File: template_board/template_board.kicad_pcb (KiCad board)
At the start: 4 copper layers, 100 x 60 mm, 150 parts, among them IC1 TJA1044GTK_3Z, IC2 TJA1044GTK_3Z, IC3 LMR16030SDDAR, J1 SWD, J2 Conn_01x02, J4 USB_C_Receptacle_USB2.0, J6 Conn_01x02, J7 RJ45_LED_Shielded, J8 RJ45_LED_Shielded, Q1 S9013, SW2 NRST, SW5 SW_DIP_x02, U1 CH334R, U2 FM24CL16B, U3 STM32F103CB, U4 AZ1117-3.3, U6 IP4220CZ6, U8 TS3USB30EDGSR, U9 STM32F446RETx, Y1 8MHz, Y2 8MHz, Y3 32.768kHz, Y4 12Mhz

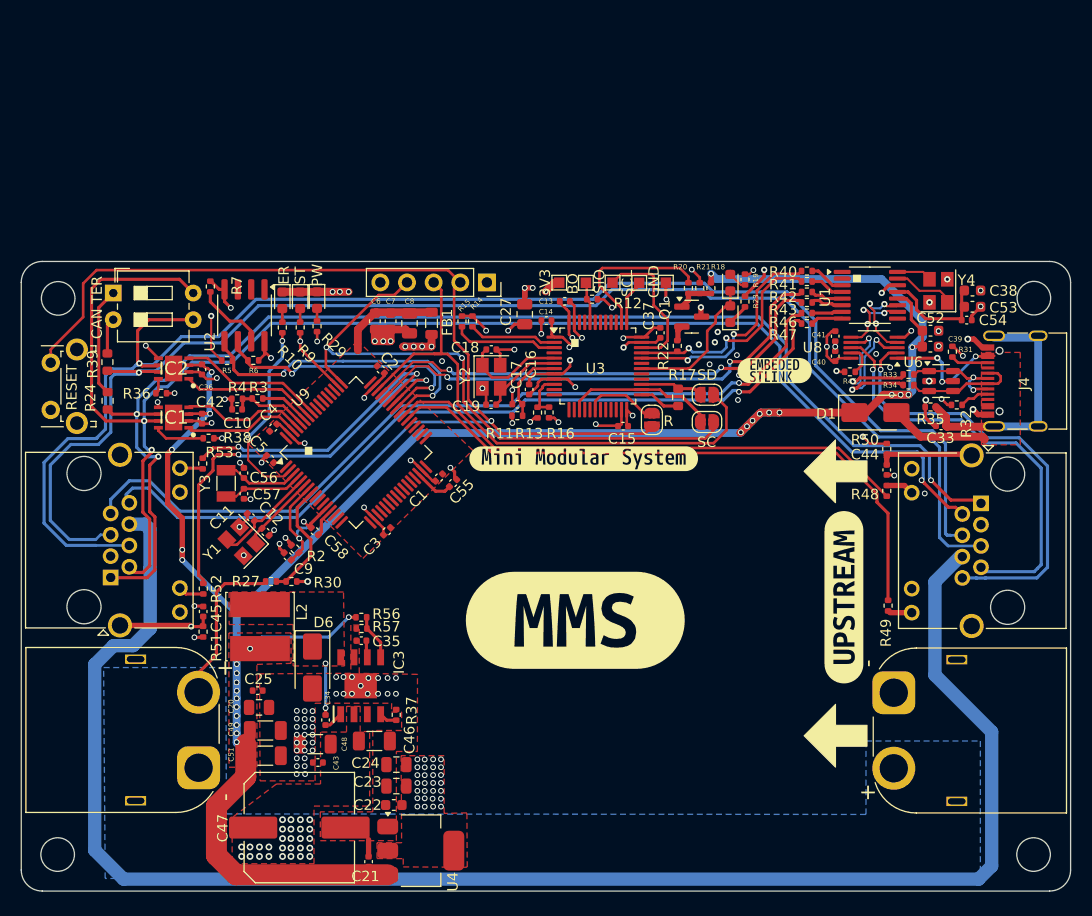
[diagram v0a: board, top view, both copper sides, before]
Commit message: updated all subschematics
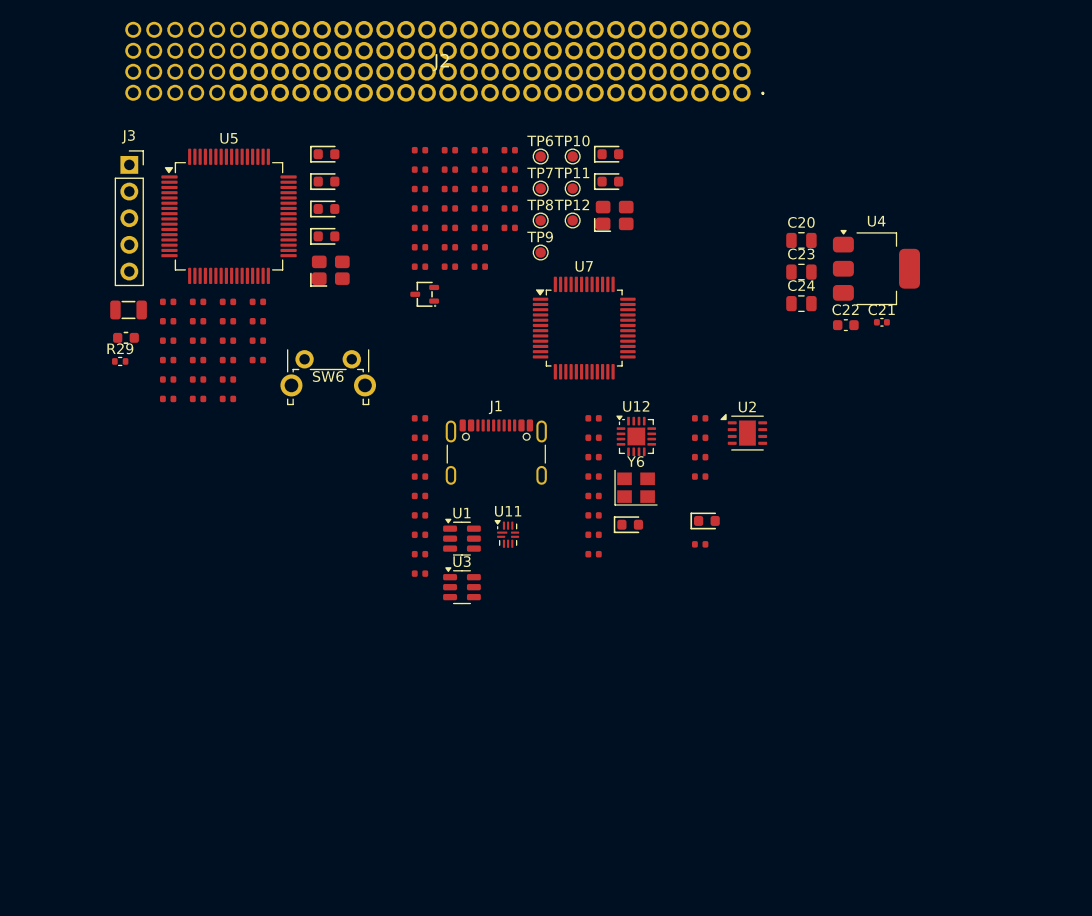
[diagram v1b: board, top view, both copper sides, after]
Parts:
- removed C11, C12: 17p, Capacitor_SMD:C_0402_1005Metric
- removed C13, C14, C15, C16, C17, C37: 100nF, Capacitor_SMD:C_0402_1005Metric
- removed C18, C19: 20pF, Capacitor_SMD:C_0402_1005Metric
- removed C27: 10u, Capacitor_SMD:C_0805_2012Metric
- removed C33: 10n, Capacitor_SMD:C_0402_1005Metric
- removed C36, C40, C42, C54: 100n, Capacitor_SMD:C_0402_1005Metric
- removed C38, C39: 10u, Capacitor_SMD:C_0603_1608Metric
- removed C41: 1n, Capacitor_SMD:C_0402_1005Metric
- removed C52: 100n, Capacitor_SMD:C_0603_1608Metric
- removed C53: 1u, Capacitor_SMD:C_0603_1608Metric
- removed C55: 2.2u, Capacitor_SMD:C_0402_1005Metric
- removed C56, C57: 6P, Capacitor_SMD:C_0402_1005Metric
- removed D1: ss34, Diode_SMD:D_SMA
- removed D4: BLUE, LED_SMD:LED_0603_1608Metric
- removed D5: RED, LED_SMD:LED_0603_1608Metric
- removed D6: SS34, Diode_SMD:D_SMA
- removed H1, H2, H3, H4: ~, MountingHole:MountingHole_3.2mm_M3
- removed IC1, IC2: TJA1044GTK_3Z, parts:SON65P300X300X100-9N-D
- removed IC3: LMR16030SDDAR, parts:SOIC127P600X170-9N
- removed J4: USB_C_Receptacle_USB2.0, Connector_USB:USB_C_Receptacle_G-Switch_GT-USB-7010ASV
- removed J6: Conn_01x02, Connector_AMASS:AMASS_XT60PW-M_1x02_P7.20mm_Horizontal
- removed J7, J8: RJ45_LED_Shielded, Connector_RJ:RJ45_Amphenol_RJHSE538X
- removed JP1, JP2, JP3: SolderJumper_2_Bridged, Jumper:SolderJumper-2_P1.3mm_Open_RoundedPad1.0x1.5mm
- removed L2: 8.2u, Inductor_SMD:L_Cenker_CKCS6045
- removed Q1: S9013, Package_TO_SOT_SMD:SOT-23
- removed R11, R12: 100k, Resistor_SMD:R_0402_1005Metric
- removed R13, R16, R31, R32: 4k7, Resistor_SMD:R_0402_1005Metric
- removed R14, R18, R36, R38, R45: 10k, Resistor_SMD:R_0402_1005Metric
- removed R15: DNP, Resistor_SMD:R_0402_1005Metric
- removed R17: 100R, Resistor_SMD:R_0603_1608Metric
- removed R19, R23: 220R, Resistor_SMD:R_0402_1005Metric
- removed R20: 100R, Resistor_SMD:R_0402_1005Metric
- removed R21: 39k, Resistor_SMD:R_0402_1005Metric
- removed R22: 1K5, Resistor_SMD:R_0402_1005Metric
- removed R24, R39: 120R, Resistor_SMD:R_0603_1608Metric
- removed R33, R34, R40, R41, R42, R43, R46, R47: 22R, Resistor_SMD:R_0402_1005Metric
- removed R35: 33k, Resistor_SMD:R_0402_1005Metric
- removed SW2: NRST, Button_Switch_THT:SW_Tactile_SPST_Angled_PTS645Vx58-2LFS
- removed SW5: SW_DIP_x02, Button_Switch_THT:SW_DIP_SPSTx02_Slide_6.7x6.64mm_W7.62mm_P2.54mm_LowProfile
- removed TP1, TP2, TP3, TP4, TP5: ~, TestPoint:TestPoint_Pad_1.0x1.0mm
- removed U6: IP4220CZ6, Package_TO_SOT_SMD:SOT-23-6
- removed U8: TS3USB30EDGSR, Package_SO:VSSOP-10_3x3mm_P0.5mm
- removed U9: STM32F446RETx, Package_QFP:LQFP-64_10x10mm_P0.5mm
- removed Y1, Y2: 8MHz, Crystal:Crystal_SMD_3225-4Pin_3.2x2.5mm
- removed Y3: 32.768kHz, Crystal:Crystal_SMD_3215-2Pin_3.2x1.5mm
- removed Y4: 12Mhz, Crystal:Crystal_SMD_3225-4Pin_3.2x2.5mm
- removed kibuzzard-673147F0 (x2): G***, kibuzzard-673147F0
- removed kibuzzard-67314807: G***, kibuzzard-67314807
- removed kibuzzard-67314D46: G***, kibuzzard-67314D46
- removed kibuzzard-673151BF: G***, kibuzzard-673151BF
- removed kibuzzard-674CE2D2: G***, kibuzzard-674CE2D2
- added C26: 100nF, PCM_JLCPCB:C_0402, F.Cu at (118.0, 58.6)
- added C28: 100nF, PCM_JLCPCB:C_0402, F.Cu at (94.0, 71.2)
- added C29: 100nF, PCM_JLCPCB:C_0402, F.Cu at (94.0, 73.1)
- added C30: 100nF, PCM_JLCPCB:C_0402, F.Cu at (96.8, 63.9)
- added C31: 1uF, PCM_JLCPCB:C_0402, F.Cu at (96.8, 65.7)
- added C32: 10nF, PCM_JLCPCB:C_0402, F.Cu at (96.8, 67.5)
- added C50: 4.7uF, PCM_JLCPCB:C_0402, F.Cu at (96.8, 69.4)
- added C59: 18pF, PCM_JLCPCB:C_0402, F.Cu at (99.7, 63.9)
- added C60: 22pF, PCM_JLCPCB:C_0402, F.Cu at (99.7, 65.7)
- added D10: Green, PCM_JLCPCB:D_0603, F.Cu at (145.3, 84.7)
- added D11: Red, PCM_JLCPCB:D_0603, F.Cu at (109.1, 55.0)
- added D12: Blue, PCM_JLCPCB:D_0603, F.Cu at (109.1, 57.6)
- added D8: Green, PCM_JLCPCB:D_0603, F.Cu at (136.1, 52.4)
- added D9: Red, PCM_JLCPCB:D_0603, F.Cu at (138.0, 85.1)
- added J3: SWD, Connector_PinSocket_2.54mm:PinSocket_1x05_P2.54mm_Vertical, F.Cu at (90.3, 50.8)
- added Q2: MMST3904, PCM_JLCPCB:Q_SOT-323, F.Cu at (118.4, 63.1)
- added R25: 100Ω, PCM_JLCPCB:R_0402, F.Cu at (120.8, 60.5)
- added R26: 10kΩ, PCM_JLCPCB:R_0402, F.Cu at (123.7, 49.4)
- added R28: 10kΩ, PCM_JLCPCB:R_0402, F.Cu at (123.7, 51.2)
- added R44: 22Ω, PCM_JLCPCB:R_0402, F.Cu at (123.7, 55.0)
- added R54: 39kΩ, PCM_JLCPCB:R_0402, F.Cu at (126.5, 55.0)
- added R55: 100Ω, PCM_JLCPCB:R_0402, F.Cu at (126.5, 56.8)
- added R58: 5.1kΩ, PCM_JLCPCB:R_0402, F.Cu at (118.0, 84.2)
- added R59: 10kΩ, PCM_JLCPCB:R_0402, F.Cu at (118.0, 86.0)
- added R60: 22kΩ, PCM_JLCPCB:R_0402, F.Cu at (118.0, 87.9)
- added R61: 10kΩ, PCM_JLCPCB:R_0402, F.Cu at (118.0, 89.8)
- added R62: 220Ω, PCM_JLCPCB:R_0402, F.Cu at (144.7, 87.0)
- added R63: 470Ω, PCM_JLCPCB:R_0402, F.Cu at (102.5, 65.7)
- added R64: 22Ω, PCM_JLCPCB:R_0402, F.Cu at (134.5, 80.5)
- added R65: 22Ω, PCM_JLCPCB:R_0402, F.Cu at (134.5, 82.3)
- added R66: 22Ω, PCM_JLCPCB:R_0402, F.Cu at (134.5, 84.2)
- added R67: 22Ω, PCM_JLCPCB:R_0402, F.Cu at (134.5, 86.0)
- added R68: 1kΩ, PCM_JLCPCB:R_0402, F.Cu at (134.5, 87.9)
- added R69: 1.2kΩ, PCM_JLCPCB:R_0402, F.Cu at (102.5, 67.5)
- added R70: 120Ω, PCM_JLCPCB:R_0402, F.Cu at (102.5, 69.4)
- added R8: 22Ω, PCM_JLCPCB:R_0402, F.Cu at (120.8, 55.0)
- added SW6: NRST, Button_Switch_THT:SW_Tactile_SPST_Angled_PTS645Vx58-2LFS, F.Cu at (107.0, 69.3)
- added TP10: ~, TestPoint:TestPoint_Pad_D1.0mm, F.Cu at (132.6, 50.0)
- added TP11: ~, TestPoint:TestPoint_Pad_D1.0mm, F.Cu at (132.6, 53.0)
- added TP12: ~, TestPoint:TestPoint_Pad_D1.0mm, F.Cu at (132.6, 56.1)
- added TP6: TestPoint, TestPoint:TestPoint_Pad_D1.0mm, F.Cu at (129.5, 50.0)
- added TP7: TestPoint, TestPoint:TestPoint_Pad_D1.0mm, F.Cu at (129.5, 53.0)
- added TP8: ~, TestPoint:TestPoint_Pad_D1.0mm, F.Cu at (129.5, 56.1)
- added TP9: ~, TestPoint:TestPoint_Pad_D1.0mm, F.Cu at (129.5, 59.1)
- added U11: FSUSB42UMX, Package_DFN_QFN:UQFN-10_1.4x1.8mm_P0.4mm, F.Cu at (126.4, 86.0)
- added U12: CH334P, Package_DFN_QFN:QFN-16-1EP_3x3mm_P0.5mm_EP1.7x1.7mm, F.Cu at (138.6, 76.7)
- added U5: STM32U575RITx, Package_QFP:LQFP-64_10x10mm_P0.5mm, F.Cu at (99.8, 55.7)
- added U7: STM32F103CBTx, Package_QFP:LQFP-48_7x7mm_P0.5mm, F.Cu at (133.7, 66.3)
- added X3: Q13FC1350000400, PCM_JLCPCB:FC-135R_L3.2-W1.5, F.Cu at (90.2, 64.6)
- added X4: X322512MSB4SI, PCM_JLCPCB:CRYSTAL-SMD_4P-L3.2-W2.5-BL, F.Cu at (109.5, 60.8)
- added Y5: 8 MHz, PCM_JLCPCB:CRYSTAL-SMD_4P-L3.2-W2.5-BL, F.Cu at (136.6, 55.6)
- added Y6: 12Mhz, Crystal:Crystal_SMD_3225-4Pin_3.2x2.5mm, F.Cu at (138.6, 81.6)
- C1: value 100n -> 4.7uF; footprint Capacitor_SMD:C_0402_1005Metric -> PCM_JLCPCB:C_0402
- C10: value 4.7u -> 100nF; footprint Capacitor_SMD:C_0402_1005Metric -> PCM_JLCPCB:C_0402
- C2, C25, C3, C34, C35, C4, C43, C5, C9: value 100n -> 100nF; footprint Capacitor_SMD:C_0402_1005Metric -> PCM_JLCPCB:C_0402
- C44, C45: value 10n -> 100nF; footprint Capacitor_SMD:C_0402_1005Metric -> PCM_JLCPCB:C_0402
- C46: value 2.2u -> 100nF; footprint Capacitor_SMD:C_1206_3216Metric -> PCM_JLCPCB:C_0402
- C47: value 47u -> 100nF; footprint Capacitor_SMD:C_Elec_10x10.2 -> PCM_JLCPCB:C_0402
- C48: value 2.2u -> 10uF; footprint Capacitor_SMD:C_1206_3216Metric -> PCM_JLCPCB:C_0402
- C49: value 47u -> 1uF; footprint Capacitor_SMD:C_1206_3216Metric -> PCM_JLCPCB:C_0402
- C51: value 47u -> 18pF; footprint Capacitor_SMD:C_1206_3216Metric -> PCM_JLCPCB:C_0402
- C58: value 100n -> 22pF; footprint Capacitor_SMD:C_0402_1005Metric -> PCM_JLCPCB:C_0402
- C6: value 1u -> 33pF; footprint Capacitor_SMD:C_0603_1608Metric -> PCM_JLCPCB:C_0402
- C7: value 4.7u -> 1uF; footprint Capacitor_SMD:C_0603_1608Metric -> PCM_JLCPCB:C_0402
- C8: value 10u -> 33pF; footprint Capacitor_SMD:C_0805_2012Metric -> PCM_JLCPCB:C_0402
- D2: value USR_LED1 -> Blue; footprint Diode_SMD:D_0603_1608Metric -> PCM_JLCPCB:D_0603
- D3: value USR_LED2 -> Blue; footprint Diode_SMD:D_0603_1608Metric -> PCM_JLCPCB:D_0603
- D7: value LV_PWR -> Red; footprint Diode_SMD:D_0603_1608Metric -> PCM_JLCPCB:D_0603
- FB1: value FerriteBead -> ~; footprint Inductor_SMD:L_0805_2012Metric -> PCM_JLCPCB:FB_0603
- J1: value SWD -> USB_C_Receptacle_USB2.0_16P; footprint Connector_PinSocket_2.54mm:PinSocket_1x05_P2.54mm_Vertical -> Connector_USB:USB_C_Receptacle_GCT_USB4105-xx-A_16P_TopMnt_Horizontal
- J2: value Conn_01x02 -> PTHF-130-02-G-Q-368; footprint Connector_AMASS:AMASS_XT60PW-M_1x02_P7.20mm_Horizontal -> lib:PTHF13002GQ368
- R10: value 1k -> 100kΩ; footprint Resistor_SMD:R_0402_1005Metric -> PCM_JLCPCB:R_0402
- R2: value 10k -> 120Ω; footprint Resistor_SMD:R_0402_1005Metric -> PCM_JLCPCB:R_0402
- R27: value 43k -> 10kΩ; footprint Resistor_SMD:R_0402_1005Metric -> PCM_JLCPCB:R_0402
- R29: value 220 -> 1k
- R3: value 1k -> 1kΩ; footprint Resistor_SMD:R_0402_1005Metric -> PCM_JLCPCB:R_0402
- R30, R52: value 1k -> 1.2kΩ; footprint Resistor_SMD:R_0402_1005Metric -> PCM_JLCPCB:R_0402
- R37: value 49,9k -> 22Ω; footprint Resistor_SMD:R_0402_1005Metric -> PCM_JLCPCB:R_0402
- R4: value 10k -> 10kΩ; footprint Resistor_SMD:R_0402_1005Metric -> PCM_JLCPCB:R_0402
- R48, R49, R53: value 1k -> 10kΩ; footprint Resistor_SMD:R_0402_1005Metric -> PCM_JLCPCB:R_0402
- R5, R6: value 4k7 -> 10kΩ; footprint Resistor_SMD:R_0402_1005Metric -> PCM_JLCPCB:R_0402
- R50, R51: value 33k -> 10kΩ; footprint Resistor_SMD:R_0402_1005Metric -> PCM_JLCPCB:R_0402
- R56: value 100k -> 330Ω; footprint Resistor_SMD:R_0402_1005Metric -> PCM_JLCPCB:R_0402
- R57: value 17,8k -> 5.1kΩ; footprint Resistor_SMD:R_0402_1005Metric -> PCM_JLCPCB:R_0402
- R7: value 10k -> 100kΩ; footprint Resistor_SMD:R_0402_1005Metric -> PCM_JLCPCB:R_0402
- R9: value 1k -> 22Ω; footprint Resistor_SMD:R_0402_1005Metric -> PCM_JLCPCB:R_0402
- U1: value CH334R -> IP4220CZ6; footprint Package_SO:QSOP-16_3.9x4.9mm_P0.635mm -> Package_TO_SOT_SMD:SOT-23-6
- U2: value FM24CL16B -> TJA1044GTK_3Z; footprint Package_SO:SOIC-8_3.9x4.9mm_P1.27mm -> Package_SON:HVSON-8-1EP_3x3mm_P0.65mm_EP1.6x2.4mm
- U3: value STM32F103CB -> IP4220CZ6; footprint Package_QFP:LQFP-48_7x7mm_P0.5mm -> Package_TO_SOT_SMD:SOT-23-6
- moved C21 71.0 mm to (162.0, 65.8), turned to 0 degrees
- moved U4 70.4 mm to (161.5, 60.7)
- moved C20 68.2 mm to (154.3, 58.0)
- moved C22 62.8 mm to (158.6, 66.1), turned to 0 degrees
- moved C23 62.4 mm to (154.3, 61.0), turned to 0 degrees
- moved J2 59.0 mm to (148.7, 43.9), turned to 0 degrees
- moved C24 58.5 mm to (154.3, 64.0), turned to 0 degrees
- moved C43 57.9 mm to (120.8, 51.2), turned to 0 degrees
- moved R51 54.4 mm to (126.5, 49.4), turned to 0 degrees
- moved R49 51.8 mm to (123.7, 58.6), turned to 0 degrees
- moved R37 50.7 mm to (123.7, 53.1), turned to 0 degrees
- moved R52 49.5 mm to (126.5, 51.2), turned to 0 degrees
- moved U2 49.2 mm to (149.2, 76.4), turned to 0 degrees
- moved C47 48.0 mm to (134.5, 75.0)
- moved C35 47.5 mm to (120.8, 49.4)
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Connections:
- C1 pad 1: /MCU/3V3_MCU -> /MCU/BOOT0
- C10 pad 1: /MCU/BOOT0 -> /MCU/+VDDA
- C2 pad 1: /MCU/3V3_MCU -> /MCU/SWD.~{RST}
- C25 pad 1: +5V -> +3V3
- C3 pad 1: /MCU/3V3_MCU -> GND
- C3 pad 2: GND -> +5V
- C34 pad 1: Net-(IC3-BOOT) -> +3V3
- C34 pad 2: /POWER/5V_COIL -> GND
- C35 pad 1: GND -> +3V3
- C35 pad 2: Net-(IC3-SS) -> GND
- C4 pad 1: /MCU/3V3_MCU -> +3V3
- C43 pad 1: VCC -> +3V3
- C44 pad 1: Net-(C44-Pad1) -> Net-(J1-SHIELD)
- C45 pad 1: Net-(C45-Pad1) -> /USB-C/VBUS_IN
- C46 pad 1: VCC -> +3V3
- C47 pad 1: VCC -> Net-(U12-3V3)
- C48 pad 1: VCC -> Net-(U12-3V3)
- C5 pad 1: /MCU/3V3_MCU -> /ST-LINK/STLINK-RST
- C51 pad 1: +5V -> /MCU/OSC32_OUT
- C58 pad 1: /MCU/3V3_MCU -> /MCU/OSC_IN
- C6 pad 1: /MCU/3V3_MCU -> /ST-LINK/STLINK-OSC_IN
- C7 pad 1: /MCU/3V3_MCU -> +3V3
- C8 pad 1: /MCU/3V3_MCU -> /ST-LINK/STLINK-OSC_OUT
- C9 pad 1: /MCU/NRST -> /MCU/+VDDA
- D2 pad 2: Net-(D2-A) -> Net-(D2-Pad2)
- D3 pad 1: GND -> /ST-LINK/LED
- D3 pad 2: Net-(D3-A) -> Net-(D3-Pad2)
- D7 pad 2: Net-(D7-A) -> Net-(D7-Pad2)
- FB1 pad 1: /MCU/3V3_MCU -> +3V3
- FB1 pad 2: +3V3 -> /MCU/+VDDA
- J2 pad 1: GND -> unconnected-(J2-Pad1)
- J2 pad 2: VCC -> unconnected-(J2-Pad2)
- R10 pad 1: /MCU/USR_LED2 -> GND
- R10 pad 2: Net-(D3-A) -> /ST-LINK/STLINK-BOOT0
- R2 pad 1: +3V3 -> /BUS_CONNECTOR/CAN1.+
- R2 pad 2: /MCU/NRST -> Net-(R2-Pad2)
- R27 pad 1: VCC -> +5V
- R29 pad 1: +3V3 -> /MCU/V_SENSE
- R29 pad 2: Net-(D7-A) -> GND
- R30 pad 1: /MCU/V_SENSE -> /MCU/USER_LED_1
- R30 pad 2: GND -> Net-(D12-Pad2)
- R37 pad 1: Net-(IC3-RT/SYNC) -> /MCU/SWD.~{RST}
- R37 pad 2: GND -> Net-(U7-PB0)
- R48 pad 1: /CAN/RXD1_LED -> +3V3
- R48 pad 2: Net-(J7-Pad10) -> Net-(U7-PA0)
- R49 pad 1: /CAN/TXD1_LED -> Net-(U7-PA0)
- R49 pad 2: Net-(J7-Pad12) -> GND
- R5 pad 2: /MCU/I2C3_SDA -> /MCU/SWD.~{RST}
- R50 pad 1: Net-(C44-Pad1) -> +3V3
- R50 pad 2: GND -> Net-(D3-Pad2)
- R51 pad 1: Net-(C45-Pad1) -> Net-(D8-Pad1)
- R52 pad 1: /CAN/RXD2_LED -> Net-(Q2-E)
- R52 pad 2: Net-(J8-Pad10) -> /ST-LINK/ST-LINK.D+
- R53 pad 1: /CAN/TXD2_LED -> +5V
- R56 pad 1: +5V -> Net-(J1-SHIELD)
- R56 pad 2: Net-(IC3-FB) -> GND
- R57 pad 1: Net-(IC3-FB) -> /USB-C/CC2
- R6 pad 1: +3V3 -> Net-(U2-STB)
- R6 pad 2: /MCU/I2C3_SCL -> GND
- R7 pad 1: GND -> +3V3
- R7 pad 2: Net-(U2-WP) -> /ST-LINK/STLINK-RST
- R9 pad 1: /MCU/USR_LED1 -> /MCU/SWD.SWDIO
- R9 pad 2: Net-(D2-A) -> Net-(U7-PB14)
- U1 pad 1: unconnected-(U1-DM4-Pad1) -> /USB-C/BACKPLANE.D-
- U1 pad 2: unconnected-(U1-DP4-Pad2) -> GND
- U1 pad 3: Net-(U1-DM3) -> /USB-C/BACKPLANE.D+
- U1 pad 4: Net-(U1-DP3) -> /USB-C/BACKPLANE.D+
- U1 pad 5: Net-(U1-DM2) -> /USB-C/VBUS_IN
- U1 pad 6: Net-(U1-DP2) -> /USB-C/BACKPLANE.D-
- U2 pad 1: unconnected-(U2-NC-Pad1) -> /MCU/CAN.TX
- U2 pad 2: unconnected-(U2-NC-Pad2) -> GND
- U2 pad 3: unconnected-(U2-NC-Pad3) -> +5V
- U2 pad 4: GND -> /MCU/CAN.RX
- U2 pad 5: /MCU/I2C3_SDA -> +3V3
- U2 pad 6: /MCU/I2C3_SCL -> /BUS_CONNECTOR/CAN1.-
- U2 pad 7: Net-(U2-WP) -> /BUS_CONNECTOR/CAN1.+
- U2 pad 8: +3V3 -> Net-(U2-STB)
- U3 pad 1: +3V3 -> /USB-C/USB2S.D-
- U3 pad 2: Net-(U3-PC13) -> GND
- U3 pad 3: Net-(U3-PC14) -> /USB-C/USB2S.D+
- U3 pad 4: unconnected-(U3-PC15-Pad4) -> /USB-C/USB2S.D+
- U3 pad 5: Net-(U3-PD0) -> /USB-C/VBUS_IN
- U3 pad 6: Net-(U3-PD1) -> /USB-C/USB2S.D-
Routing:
- net +5V: track 202.8 -> 0.00 mm, vias 28 -> 0
- net +12V: track 156.1 -> 0.00 mm
- net /CAN/CAN2-: track 141.1 -> 0.00 mm, vias 1 -> 0
- net /CAN/CAN1+: track 140.0 -> 0.00 mm, vias 3 -> 0
- net /CAN/CAN2+: track 133.3 -> 0.00 mm, vias 1 -> 0
- net GND: track 122.6 -> 0.00 mm, vias 113 -> 0
- net /CAN/CAN1-: track 122.2 -> 0.00 mm, vias 3 -> 0
- net /MCU/NRST: track 109.0 -> 0.00 mm, vias 2 -> 0
- net /CAN/USB_DOWNSTREAM_D-: track 78.4 -> 0.00 mm, vias 1 -> 0
- net /CAN/USB_DOWNSTREAM_D+: track 76.1 -> 0.00 mm, vias 1 -> 0
- net /CAN/TXD1_LED: track 59.2 -> 0.00 mm
- net /MCU/SWCLK: track 58.8 -> 0.00 mm, vias 2 -> 0
- net /MCU/SWDIO: track 53.3 -> 0.00 mm
- net /CAN/RXD1_LED: track 50.3 -> 0.00 mm
- net +3V3: track 49.6 -> 0.00 mm, vias 50 -> 0
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- removed copper zone on F.Cu, net +3V3
- removed copper zone on F.Cu, net +5V
- removed copper zone on F.Cu, net /MCU/3V3_MCU
- removed copper zone on F.Cu, net /POWER/5V_COIL
- removed copper zone on F.Cu, net /USB/VBUS
- removed copper zone on F.Cu, net GND
- removed copper zone on B.Cu, net VCC
- removed copper zone on F.Cu, net VCC
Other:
- board outline removed
- board text removed: "."
- board text removed: "12V"
- board text removed: "3V3"
- board text removed: "BO"
- board text removed: "C1+"
- board text removed: "C1-"
- board text removed: "C2+"
- board text removed: "C2-"
- board text removed: "CAN TER"
- board text removed: "D+"
- board text removed: "D-"
- board text removed: "ER"
- board text removed: "GND"
- board text removed: "MMS Mini Modular System designed by Patryk Dudziński REV1.0 11.11.2024"
- board text removed: "NRESET"
- board text removed: "PW"
- board text removed: "QC"
- board text removed: "R"
- board text removed: "RESET"
- board text removed: "S/N"
- board text removed: "SC"
- board text removed: "SCL"
- board text removed: "SD"
- board text removed: "SIO"
- board text removed: "ST"

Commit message: update pcb leyout goruping
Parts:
- removed TP10, TP11, TP12, TP8, TP9: ~, TestPoint:TestPoint_Pad_D1.0mm
- added J4: SWD, Connector_PinSocket_2.54mm:PinSocket_1x05_P2.54mm_Vertical, F.Cu at (247.2, 119.6)
- moved R51 120.8 mm to (231.6, 109.0)
- moved R52 120.8 mm to (231.6, 110.9)
- moved R53 120.8 mm to (231.6, 112.8)
- moved R54 120.8 mm to (231.6, 114.6)
- moved R55 120.8 mm to (231.6, 116.5)
- moved C25 120.8 mm to (223.0, 116.5)
- moved C26 120.8 mm to (223.0, 118.3)
- moved C34 120.8 mm to (223.0, 120.2)
- moved C35 120.8 mm to (225.8, 109.0)
- moved C43 120.8 mm to (225.8, 110.9)
- moved C5 120.8 mm to (223.0, 109.0)
- moved C6 120.8 mm to (223.0, 110.9)
- moved C7 120.8 mm to (223.0, 112.8)
- moved C8 120.8 mm to (223.0, 114.6)
- moved D3 120.8 mm to (241.1, 109.4)
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
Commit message: chamt skończony chyba
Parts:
- removed C20, C23, C24: 10u, Capacitor_SMD:C_0805_2012Metric
- removed C21: 100n, Capacitor_SMD:C_0402_1005Metric
- removed C22: 100n, Capacitor_SMD:C_0603_1608Metric
- removed C4: 100nF, PCM_JLCPCB:C_0402
- removed D11: Red, PCM_JLCPCB:D_0603
- removed R6: 10kΩ, PCM_JLCPCB:R_0402
- removed R70: 120Ω, PCM_JLCPCB:R_0402
- removed SW6: NRST, Button_Switch_THT:SW_Tactile_SPST_Angled_PTS645Vx58-2LFS
- added C11: 10uF, PCM_JLCPCB:C_0402, F.Cu at (181.2, 128.5)
- added C12: 100nF, PCM_JLCPCB:C_0402, F.Cu at (181.2, 130.4)
- added C13: 100nF, PCM_JLCPCB:C_0402, F.Cu at (181.2, 132.2)
- added C14: 10uF, PCM_JLCPCB:C_0402, F.Cu at (181.2, 134.1)
- added C15: 10uF, PCM_JLCPCB:C_0402, F.Cu at (181.2, 135.9)
- added C16: 100nF 50V Y5V, Capacitor_SMD:C_0402_1005Metric, F.Cu at (189.2, 141.5)
- added C17: 100nF, PCM_JLCPCB:C_0402, F.Cu at (132.5, 136.0)
- added C18: 100nF, PCM_JLCPCB:C_0402, F.Cu at (132.5, 137.8)
- added D1: Green, PCM_JLCPCB:D_0603, F.Cu at (194.5, 128.9)
- added Q3: AO3400A, Package_TO_SOT_SMD:SOT-23, F.Cu at (190.2, 138.3)
- added R1: 220Ω, PCM_JLCPCB:R_0402, F.Cu at (181.2, 137.8)
- added R11: 10kΩ, PCM_JLCPCB:R_0402, F.Cu at (181.2, 139.6)
- added R12: 10kΩ, PCM_JLCPCB:R_0402, F.Cu at (132.5, 141.5)
- added R13: 10kΩ, PCM_JLCPCB:R_0402, F.Cu at (132.5, 143.4)
- added R14: 1kΩ, PCM_JLCPCB:R_0402, F.Cu at (181.2, 141.5)
- added SW1: SW_Push, lib:TS1088R02026, F.Cu at (69.8, 83.5)
- added SW2: SW_DIP_x01, Button_Switch_THT:SW_DIP_SPSTx01_Slide_9.78x4.72mm_W7.62mm_P2.54mm, F.Cu at (133.0, 130.0)
- added SW3: SW_Push, lib:TS1088R02026, F.Cu at (146.7, 136.2)
- added U6: TJA1145T, Package_SO:SOIC-14_3.9x8.7mm_P1.27mm, F.Cu at (138.2, 138.4)
- U2: value TJA1044GTK_3Z -> LM74700; footprint Package_SON:HVSON-8-1EP_3x3mm_P0.65mm_EP1.6x2.4mm -> Package_TO_SOT_SMD:SOT-23-6
- moved J4 191.5 mm to (56.0, 130.9)
- moved J1 176.6 mm to (229.5, 71.3)
- moved U11 176.6 mm to (230.7, 78.1)
- moved C44 176.6 mm to (222.2, 67.0)
- moved C45 176.6 mm to (222.2, 68.8)
- moved C46 176.6 mm to (222.2, 70.7)
- moved R56 176.6 mm to (222.2, 72.5)
- moved R57 176.6 mm to (222.2, 74.4)
- moved R58 176.6 mm to (222.2, 76.2)
- moved R59 176.6 mm to (222.2, 78.1)
- moved R60 176.6 mm to (222.2, 79.9)
- moved R61 176.6 mm to (222.2, 81.8)
- moved U1 176.6 mm to (226.2, 78.4)
- moved U3 176.6 mm to (226.2, 83.1)
- moved U7 175.9 mm to (64.0, 147.2)
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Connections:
- C3 pad 1: GND -> /can_tranciver/WAKE
- C3 pad 2: +5V -> GND
- J2 pad 1: unconnected-(J2-Pad1) -> GND
- J2 pad 10: unconnected-(J2-Pad10) -> +VREZ
- J2 pad 100: unconnected-(J2-Pad100) -> /BUS_CONNECTOR/GPIO19
- J2 pad 101: unconnected-(J2-Pad101) -> /BUS_CONNECTOR/GPIO20
- J2 pad 102: unconnected-(J2-Pad102) -> /BUS_CONNECTOR/GPIO21
- J2 pad 103: unconnected-(J2-Pad103) -> /BUS_CONNECTOR/GPIO22
- J2 pad 104: unconnected-(J2-Pad104) -> /BUS_CONNECTOR/GPIO23
- J2 pad 105: unconnected-(J2-Pad105) -> /BUS_CONNECTOR/GPIO24
- J2 pad 106: unconnected-(J2-Pad106) -> /BUS_CONNECTOR/GPIO25
- J2 pad 107: unconnected-(J2-Pad107) -> /BUS_CONNECTOR/GPIO26
- J2 pad 108: unconnected-(J2-Pad108) -> /BUS_CONNECTOR/GPIO27
- J2 pad 109: unconnected-(J2-Pad109) -> /BUS_CONNECTOR/GPIO28
- J2 pad 11: unconnected-(J2-Pad11) -> +VREZ
- J2 pad 110: unconnected-(J2-Pad110) -> /BUS_CONNECTOR/GPIO29
- J2 pad 111: unconnected-(J2-Pad111) -> /BUS_CONNECTOR/GPIO30
- J2 pad 112: unconnected-(J2-Pad112) -> /BUS_CONNECTOR/GPIO31
- J2 pad 113: unconnected-(J2-Pad113) -> /BUS_CONNECTOR/GPIO32
- J2 pad 114: unconnected-(J2-Pad114) -> /BUS_CONNECTOR/GPIO33
- J2 pad 115: unconnected-(J2-Pad115) -> /BUS_CONNECTOR/GPIO34
- J2 pad 116: unconnected-(J2-Pad116) -> /BUS_CONNECTOR/GPIO35
- J2 pad 12: unconnected-(J2-Pad12) -> +VREZ
- J2 pad 13: unconnected-(J2-Pad13) -> GND
- J2 pad 14: unconnected-(J2-Pad14) -> GND
- J2 pad 15: unconnected-(J2-Pad15) -> GND
- J2 pad 16: unconnected-(J2-Pad16) -> GND
- J2 pad 17: unconnected-(J2-Pad17) -> +VCC
- J2 pad 18: unconnected-(J2-Pad18) -> +VCC
- J2 pad 19: unconnected-(J2-Pad19) -> +VCC
- J2 pad 2: unconnected-(J2-Pad2) -> GND
- J2 pad 20: unconnected-(J2-Pad20) -> +VCC
- J2 pad 21: unconnected-(J2-Pad21) -> +VCC
- J2 pad 22: unconnected-(J2-Pad22) -> +VCC
- J2 pad 23: unconnected-(J2-Pad23) -> +VCC
- J2 pad 24: unconnected-(J2-Pad24) -> +VCC
- J2 pad 25: unconnected-(J2-Pad25) -> GND
- J2 pad 26: unconnected-(J2-Pad26) -> GND
- J2 pad 27: unconnected-(J2-Pad27) -> GND
- J2 pad 28: unconnected-(J2-Pad28) -> GND
- J2 pad 29: unconnected-(J2-Pad29) -> +5V_unprotected
- J2 pad 3: unconnected-(J2-Pad3) -> GND
- J2 pad 30: GND -> +5V_unprotected
- J2 pad 31: unconnected-(J2-Pad31) -> +5V_unprotected
- J2 pad 32: unconnected-(J2-Pad32) -> +5V_unprotected
- J2 pad 33: unconnected-(J2-Pad33) -> +5V_unprotected
- J2 pad 34: unconnected-(J2-Pad34) -> +5V_unprotected
- J2 pad 35: unconnected-(J2-Pad35) -> +5V_unprotected
- J2 pad 36: unconnected-(J2-Pad36) -> +5V_unprotected
- J2 pad 37: unconnected-(J2-Pad37) -> GND
- J2 pad 38: unconnected-(J2-Pad38) -> GND
- J2 pad 39: unconnected-(J2-Pad39) -> GND
- J2 pad 4: unconnected-(J2-Pad4) -> GND
- J2 pad 40: unconnected-(J2-Pad40) -> GND
- J2 pad 41: unconnected-(J2-Pad41) -> /BUS_CONNECTOR/CAN1.+
- J2 pad 42: unconnected-(J2-Pad42) -> /BUS_CONNECTOR/CAN2.+
- J2 pad 43: unconnected-(J2-Pad43) -> /BUS_CONNECTOR/CAN3.+
- J2 pad 44: unconnected-(J2-Pad44) -> /BUS_CONNECTOR/CAN4.+
- J2 pad 45: unconnected-(J2-Pad45) -> /BUS_CONNECTOR/CAN1.-
- J2 pad 46: unconnected-(J2-Pad46) -> /BUS_CONNECTOR/CAN2.-
- J2 pad 47: unconnected-(J2-Pad47) -> /BUS_CONNECTOR/CAN3.-
- J2 pad 48: unconnected-(J2-Pad48) -> /BUS_CONNECTOR/CAN4.-
- J2 pad 49: unconnected-(J2-Pad49) -> GND
- J2 pad 5: unconnected-(J2-Pad5) -> +VREZ
- J2 pad 50: unconnected-(J2-Pad50) -> GND
- J2 pad 51: unconnected-(J2-Pad51) -> GND
- J2 pad 52: unconnected-(J2-Pad52) -> GND
- J2 pad 53: unconnected-(J2-Pad53) -> /BUS_CONNECTOR/USB1.D+
- J2 pad 54: unconnected-(J2-Pad54) -> /BUS_CONNECTOR/USB2.D+
- J2 pad 55: unconnected-(J2-Pad55) -> /BUS_CONNECTOR/USB3.D+
- J2 pad 56: unconnected-(J2-Pad56) -> /BUS_CONNECTOR/USB4.D+
- J2 pad 57: unconnected-(J2-Pad57) -> /BUS_CONNECTOR/USB1.D-
- J2 pad 58: unconnected-(J2-Pad58) -> /BUS_CONNECTOR/USB2.D-
- J2 pad 59: unconnected-(J2-Pad59) -> /BUS_CONNECTOR/USB3.D-
- J2 pad 6: unconnected-(J2-Pad6) -> +VREZ
- J2 pad 60: unconnected-(J2-Pad60) -> /BUS_CONNECTOR/USB4.D-
- J2 pad 61: unconnected-(J2-Pad61) -> /BUS_CONNECTOR/USB5.D+
- J2 pad 62: unconnected-(J2-Pad62) -> /BUS_CONNECTOR/USB6.D+
- J2 pad 63: unconnected-(J2-Pad63) -> /BUS_CONNECTOR/USB7.D+
- J2 pad 64: unconnected-(J2-Pad64) -> /BUS_CONNECTOR/USB8.D+
- J2 pad 65: unconnected-(J2-Pad65) -> /BUS_CONNECTOR/USB5.D-
- J2 pad 66: unconnected-(J2-Pad66) -> /BUS_CONNECTOR/USB6.D-
- J2 pad 67: unconnected-(J2-Pad67) -> /BUS_CONNECTOR/USB7.D-
- J2 pad 68: unconnected-(J2-Pad68) -> /BUS_CONNECTOR/USB8.D-
- J2 pad 69: unconnected-(J2-Pad69) -> /BUS_CONNECTOR/USB9.D+
- J2 pad 7: unconnected-(J2-Pad7) -> +VREZ
- J2 pad 70: unconnected-(J2-Pad70) -> /BUS_CONNECTOR/USB10.D+
- J2 pad 71: unconnected-(J2-Pad71) -> /BUS_CONNECTOR/USB11.D+
- J2 pad 72: unconnected-(J2-Pad72) -> /BUS_CONNECTOR/USB12.D+
- J2 pad 73: unconnected-(J2-Pad73) -> /BUS_CONNECTOR/USB9.D-
- J2 pad 74: unconnected-(J2-Pad74) -> /BUS_CONNECTOR/USB10.D-
- J2 pad 75: unconnected-(J2-Pad75) -> /BUS_CONNECTOR/USB11.D-
- J2 pad 76: unconnected-(J2-Pad76) -> /BUS_CONNECTOR/USB12.D-
- J2 pad 77: unconnected-(J2-Pad77) -> GND
- J2 pad 78: unconnected-(J2-Pad78) -> GND
- J2 pad 79: unconnected-(J2-Pad79) -> GND
- J2 pad 8: unconnected-(J2-Pad8) -> +VREZ
- J2 pad 80: unconnected-(J2-Pad80) -> GND
- J2 pad 81: unconnected-(J2-Pad81) -> /BUS_CONNECTOR/GPIO0
- J2 pad 82: unconnected-(J2-Pad82) -> /BUS_CONNECTOR/GPIO1
- J2 pad 83: unconnected-(J2-Pad83) -> /BUS_CONNECTOR/GPIO2
- J2 pad 84: unconnected-(J2-Pad84) -> /BUS_CONNECTOR/GPIO3
- J2 pad 85: unconnected-(J2-Pad85) -> /BUS_CONNECTOR/GPIO4
- J2 pad 86: unconnected-(J2-Pad86) -> /BUS_CONNECTOR/GPIO5
- J2 pad 87: unconnected-(J2-Pad87) -> /BUS_CONNECTOR/GPIO6
- J2 pad 88: unconnected-(J2-Pad88) -> /BUS_CONNECTOR/GPIO7
- J2 pad 89: unconnected-(J2-Pad89) -> /BUS_CONNECTOR/GPIO8
- J2 pad 9: unconnected-(J2-Pad9) -> +VREZ
- J2 pad 90: unconnected-(J2-Pad90) -> /BUS_CONNECTOR/GPIO9
- J2 pad 91: unconnected-(J2-Pad91) -> /BUS_CONNECTOR/GPIO10
- J2 pad 92: unconnected-(J2-Pad92) -> /BUS_CONNECTOR/GPIO11
- J2 pad 93: unconnected-(J2-Pad93) -> /BUS_CONNECTOR/GPIO12
- J2 pad 94: unconnected-(J2-Pad94) -> /BUS_CONNECTOR/GPIO13
- J2 pad 95: unconnected-(J2-Pad95) -> /BUS_CONNECTOR/GPIO14
- J2 pad 96: unconnected-(J2-Pad96) -> /BUS_CONNECTOR/GPIO15
- J2 pad 97: unconnected-(J2-Pad97) -> /BUS_CONNECTOR/GPIO16
- J2 pad 98: unconnected-(J2-Pad98) -> /BUS_CONNECTOR/GPIO17
- J2 pad 99: unconnected-(J2-Pad99) -> /BUS_CONNECTOR/GPIO18
- J4 pad 1: +3V3 -> unconnected-(J4-Pin_1-Pad1)
- J4 pad 2: /ST-LINK/STLINK-BOOT0 -> unconnected-(J4-Pin_2-Pad2)
- J4 pad 3: /ST-LINK/DIO -> unconnected-(J4-Pin_3-Pad3)
- J4 pad 4: /ST-LINK/CLK -> unconnected-(J4-Pin_4-Pad4)
- J4 pad 5: GND -> unconnected-(J4-Pin_5-Pad5)
- U2 pad 1: /MCU/CAN.TX -> Net-(U2-VCAP)
- U2 pad 3: +5V -> Net-(U2-EN)
- U2 pad 4: /MCU/CAN.RX -> +5V
- U2 pad 5: +3V3 -> Net-(Q3-G)
- U2 pad 6: /BUS_CONNECTOR/CAN1.- -> +5V_unprotected
- U5 pad 55: unconnected-(U5-PB3-Pad55) -> /MCU/CAN_TRANSIVER.CLK
- U5 pad 56: unconnected-(U5-PB4-Pad56) -> /MCU/CAN_TRANSIVER.MISO
- U5 pad 57: unconnected-(U5-PB5-Pad57) -> /MCU/CAN_TRANSIVER.MOSI
- U5 pad 58: unconnected-(U5-PB6-Pad58) -> /MCU/CAN_TRANSIVER.CS
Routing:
- removed copper zone on In2.Cu, net +3V3
- removed copper zone on In1.Cu, net GND

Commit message: schemat skończony
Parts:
- removed TP6, TP7: TestPoint, TestPoint:TestPoint_Pad_D1.0mm
- moved U5 30.2 mm to (63.2, 103.4)
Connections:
- U5 pad 51: unconnected-(U5-PC10-Pad51) -> /MCU/STLINK_UART.RX
- U5 pad 52: unconnected-(U5-PC11-Pad52) -> /MCU/STLINK_UART.TX
- U7 pad 12: /ST-LINK/STLINK_TX -> /MCU/STLINK_UART.TX
- U7 pad 13: /ST-LINK/STLINK_RX -> /MCU/STLINK_UART.RX

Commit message: stated leyout
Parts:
- removed J3: SWD, Connector_PinSocket_2.54mm:PinSocket_1x05_P2.54mm_Vertical
- removed R29: 1k, Resistor_SMD:R_0402_1005Metric
- added C4: 100nF, PCM_JLCPCB:C_0402, F.Cu at (100.7, 81.9)
- added R6: 1kΩ, PCM_JLCPCB:R_0402, F.Cu at (95.9, 91.0)
- moved SW3 107.6 mm to (118.1, 32.5)
- moved C17 99.0 mm to (101.3, 42.0)
- moved C3 99.0 mm to (101.3, 40.1)
- moved R13 99.0 mm to (101.3, 49.4)
- moved SW2 99.0 mm to (101.8, 36.0)
- moved C18 99.0 mm to (101.3, 43.8)
- moved R2 99.0 mm to (101.3, 45.7)
- moved R12 99.0 mm to (101.3, 47.5)
- moved U6 94.6 mm to (109.1, 48.5), turned to 90 degrees
- moved D2 69.4 mm to (123.7, 85.7), turned to 180 degrees
- moved D12 69.4 mm to (123.7, 84.1), turned to 180 degrees
- moved D7 69.4 mm to (123.7, 87.3), turned to 180 degrees
- moved C16 57.3 mm to (147.9, 101.7)
- moved R69 56.5 mm to (120.1, 85.6)
- moved C11 56.3 mm to (141.1, 89.0)
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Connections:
- C1 pad 1: /MCU/BOOT0 -> /MCU/BOOT
- R3 pad 2: /MCU/BOOT0 -> /MCU/BOOT
- R4 pad 1: /MCU/BOOT0 -> /MCU/BOOT
- U5 pad 41: unconnected-(U5-PA8-Pad41) -> /MCU/STATUS_LED
- U5 pad 42: unconnected-(U5-PA9-Pad42) -> /MCU/USER_LED_2
- U5 pad 43: unconnected-(U5-PA10-Pad43) -> /MCU/USER_LED_1
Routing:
- net GND: track 0.00 -> 28.0 mm, vias 0 -> 19
- net /MCU/+VDDA: track 0.00 -> 16.9 mm, vias 0 -> 10
- net +3V3: track 0.00 -> 7.44 mm, vias 0 -> 7
- net /MCU/V_SENSE: track 0.00 -> 7.44 mm
- net /MCU/OSC_IN: track 0.00 -> 7.38 mm
- net /MCU/OSC32_IN: track 0.00 -> 6.85 mm
- net /MCU/SWD.~{RST}: track 0.00 -> 6.83 mm
- net /MCU/OSC32_OUT: track 0.00 -> 6.03 mm
- net /MCU/OSC_OUT: track 0.00 -> 5.70 mm
- net /ST-LINK/STLINK-OSC_IN: track 0.00 -> 4.81 mm
- net /ST-LINK/STLINK-OSC_OUT: track 0.00 -> 3.13 mm
- net Net-(U5-VCAP): track 0.00 -> 1.59 mm
- added copper zone on F.Cu, net +3V3
- added copper zone on F.Cu, net /MCU/+VDDA
- added copper zone on In2.Cu, net /MCU/+VDDA
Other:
- board outline added: 100 x 100 mm
